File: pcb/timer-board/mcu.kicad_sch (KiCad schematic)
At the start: 20 parts, among them J11 Programming connector, SW1 SW_KMR211NGLFS, SW2 SW_KMR211NGLFS, SW3 SW_KMR211NGLFS, SW4 SW_KMR211NGLFS, U1 STM32F411RET6, Y1 X322512MSB4SI

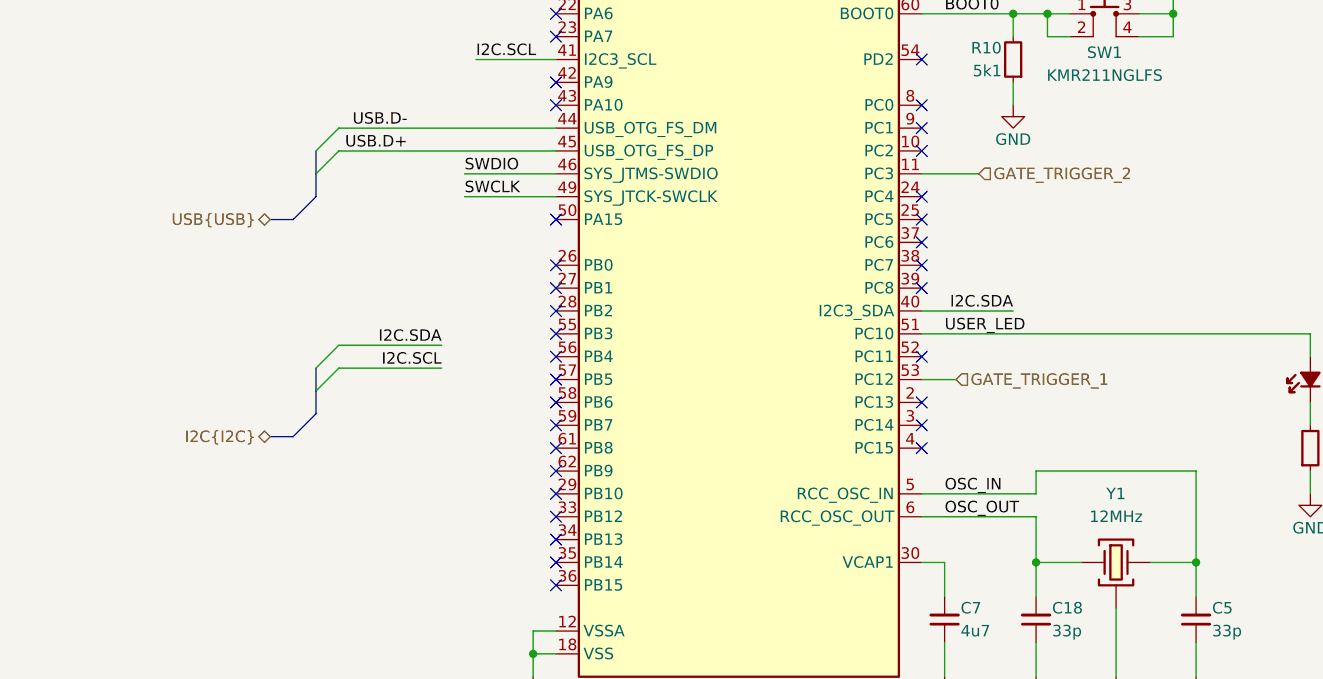
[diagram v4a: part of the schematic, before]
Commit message: Add I2C pull-up, IR receiver decoupling, LED labels, clear ERC and DRC
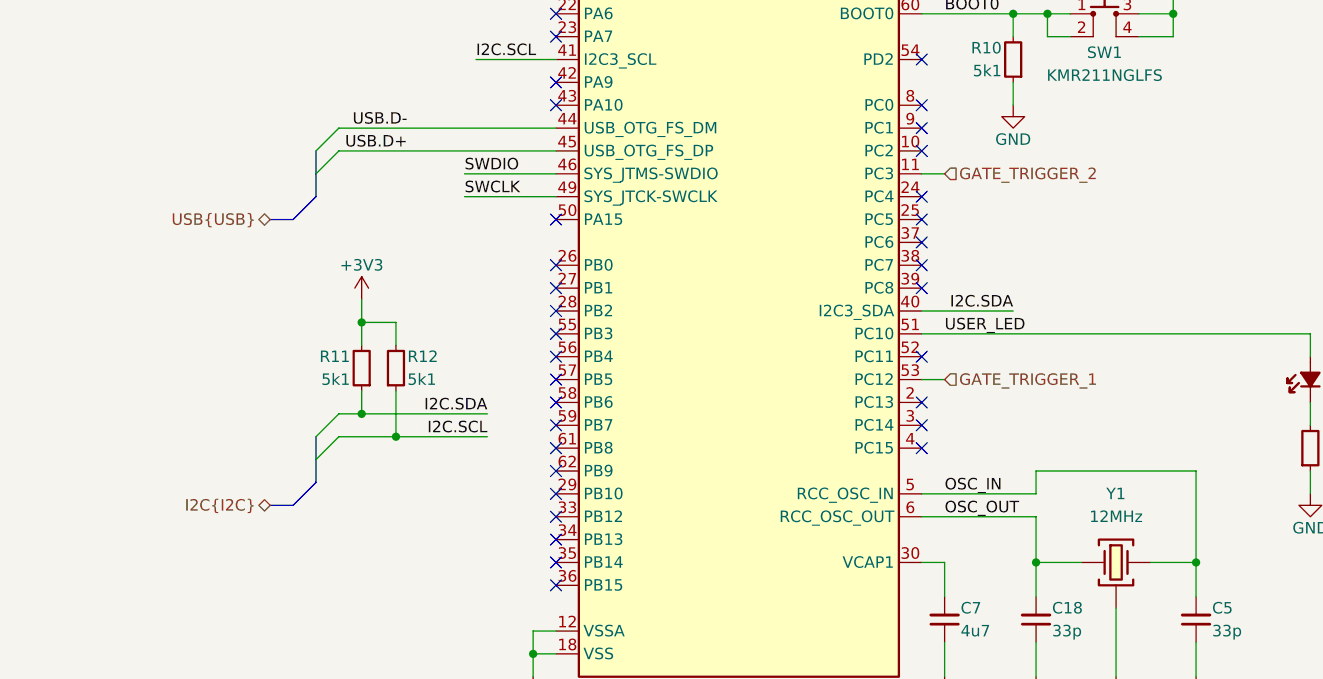
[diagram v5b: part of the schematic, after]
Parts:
- added R11, R12: R-5k1-0402, DW-footprints:R_0402_1005Metric, symbol DW-resistors:R-5k1-0402
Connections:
- net +3V3: now also R11.2, R12.2
- net I2C.SCL: now also R12.1
- net I2C.SDA: now also R11.1
